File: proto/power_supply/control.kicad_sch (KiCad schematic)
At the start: 9 parts, among them J301 Conn_01x04, J302 Conn_01x08, J303 Conn_ARM_JTAG_SWD_20, SW301 SW_Push_Dual, U301 STM32G051C6Tx

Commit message: Finish alim sch, start PCB
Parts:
- SW301: symbol Switch:SW_Push_Dual -> Switch:SW_Push
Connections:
- net GND: no longer SW301.3
- net ~{RST}: no longer SW301.4
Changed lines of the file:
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@@
 (kicad_sch (version 20230221) (generator eeschema)
   (paper "A4")
-  (junction (at 115.57 71.12) (diameter 0) (color 0 0 0 0)
-  )
   (junction (at 166.37 30.48) (diameter 0) (color 0 0 0 0)
   )
@@
   (junction (at 73.025 175.26) (diameter 0) (color 0 0 0 0)
   )
-  (junction (at 115.57 57.15) (diameter 0) (color 0 0 0 0)
-  )
   (junction (at 113.03 57.15) (diameter 0) (color 0 0 0 0)
   )
@@
     (stroke (width 0) (type default))
   )
-  (wire (pts (xy 115.57 57.15) (xy 113.03 57.15))
-    (stroke (width 0) (type default))
-  )
   (wire (pts (xy 180.34 62.23) (xy 203.2 62.23))
     (stroke (width 0) (type default))
@@
     (stroke (width 0) (type default))
   )
-  (wire (pts (xy 115.57 71.12) (xy 123.19 71.12))
-    (stroke (width 0) (type default))
-  )
-  (wire (pts (xy 115.57 57.15) (xy 123.19 57.15))
+  (wire (pts (xy 113.03 57.15) (xy 123.19 57.15))
     (stroke (width 0) (type default))
   )
@@
     (stroke (width 0) (type default))
   )
-  (wire (pts (xy 115.57 69.85) (xy 115.57 71.12))
-    (stroke (width 0) (type default))
-  )
   (wire (pts (xy 142.24 52.07) (xy 149.86 52.07))
     (stroke (width 0) (type default))
@@
     (stroke (width 0) (type default))
   )
-  (wire (pts (xy 115.57 57.15) (xy 115.57 59.69))
-    (stroke (width 0) (type default))
-  )
-  (wire (pts (xy 113.03 71.12) (xy 115.57 71.12))
+  (wire (pts (xy 113.03 71.12) (xy 123.19 71.12))
     (stroke (width 0) (type default))
   )
@@
   (symbol (lib_id "power:+3.3V") (at 173.99 25.4 0) (unit 1)
     (in_bom yes) (on_board yes) (dnp no) (fields_autoplaced)
-    (property "Reference" "#PWR0113" (at 173.99 29.21 0)
+    (property "Reference" "#PWR0301" (at 173.99 29.21 0)
       (effects (font (size 1.27 1.27)) hide)
     )
@@
       (project "power_supply"
         (path "/e87df9ac-84db-475c-955a-f1fa477bbb69/0fb30068-80ae-483e-9171-72d32f48949d"
-          (reference "#PWR0113") (unit 1)
+          (reference "#PWR0301") (unit 1)
         )
       )
@@
   (symbol (lib_id "power:+3.3V") (at 113.03 44.45 0) (unit 1)
     (in_bom yes) (on_board yes) (dnp no) (fields_autoplaced)
-    (property "Reference" "#PWR0116" (at 113.03 48.26 0)
+    (property "Reference" "#PWR0306" (at 113.03 48.26 0)
       (effects (font (size 1.27 1.27)) hide)
     )
@@
       (project "power_supply"
         (path "/e87df9ac-84db-475c-955a-f1fa477bbb69/0fb30068-80ae-483e-9171-72d32f48949d"
-          (reference "#PWR0116") (unit 1)
+          (reference "#PWR0306") (unit 1)
         )
       )
@@
   (symbol (lib_id "power:+3.3V") (at 186.69 25.4 0) (unit 1)
     (in_bom yes) (on_board yes) (dnp no) (fields_autoplaced)
-    (property "Reference" "#PWR0114" (at 186.69 29.21 0)
+    (property "Reference" "#PWR0302" (at 186.69 29.21 0)
       (effects (font (size 1.27 1.27)) hide)
     )
@@
       (project "power_supply"
         (path "/e87df9ac-84db-475c-955a-f1fa477bbb69/0fb30068-80ae-483e-9171-72d32f48949d"
-          (reference "#PWR0114") (unit 1)
+          (reference "#PWR0302") (unit 1)
         )
       )
@@
   (symbol (lib_id "power:+3.3V") (at 50.8 138.43 0) (unit 1)
     (in_bom yes) (on_board yes) (dnp no) (fields_autoplaced)
-    (property "Reference" "#PWR0117" (at 50.8 142.24 0)
+    (property "Reference" "#PWR0310" (at 50.8 142.24 0)
       (effects (font (size 1.27 1.27)) hide)
     )
@@
       (project "power_supply"
         (path "/e87df9ac-84db-475c-955a-f1fa477bbb69/0fb30068-80ae-483e-9171-72d32f48949d"
-          (reference "#PWR0117") (unit 1)
+          (reference "#PWR0310") (unit 1)
         )
       )
@@
   (symbol (lib_id "power:+3.3V") (at 166.37 26.67 0) (unit 1)
     (in_bom yes) (on_board yes) (dnp no) (fields_autoplaced)
-    (property "Reference" "#PWR0115" (at 166.37 30.48 0)
+    (property "Reference" "#PWR0303" (at 166.37 30.48 0)
       (effects (font (size 1.27 1.27)) hide)
     )
@@
       (project "power_supply"
         (path "/e87df9ac-84db-475c-955a-f1fa477bbb69/0fb30068-80ae-483e-9171-72d32f48949d"
-          (reference "#PWR0115") (unit 1)
+          (reference "#PWR0303") (unit 1)
         )
       )
@@
     )
   )
-  (symbol (lib_id "Switch:SW_Push_Dual") (at 110.49 64.77 90) (unit 1)
+  (symbol (lib_id "Switch:SW_Push") (at 110.49 64.77 90) (unit 1)
     (in_bom yes) (on_board yes) (dnp no) (fields_autoplaced)
     (property "Reference" "SW301" (at 106.68 64.135 90)
@@
     (pin "1")
     (pin "2")
-    (pin "3")
-    (pin "4")
-    (instances
-      (project "power_supply"
+    (instances
+      (project "power_supply"

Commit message: Improve overall
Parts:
- added C304, C305: C, Capacitor_SMD:C_0805_2012Metric, symbol Device:C
- added J304: Conn_01x03, Connector_PinHeader_2.54mm:PinHeader_1x03_P2.54mm_Horizontal, symbol Connector_Generic:Conn_01x03
- added R302: 0, Resistor_SMD:R_0805_2012Metric, symbol Device:R
- added Y301: 8MHz, Crystal:Crystal_SMD_5032-2Pin_5.0x3.2mm, symbol Device:Crystal
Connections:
- net GND: now also C304.2, C305.2, J304.1 (Pin_1)
- net at U301.29 (PA9/NC): now also J304.3 (Pin_3)
- net at U301.32 (PA10/NC): now also J304.2 (Pin_2)
- net at U301.8 (PF0): now also C305.1, Y301.2
- net at U301.9 (PF1): now also R302.2
- new net: C304.1, R302.1, Y301.1

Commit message: Final edit before v1 release
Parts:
- added D301, D302, D303, D304: LED, LED_SMD:LED_0805_2012Metric, symbol Device:LED
- added R303, R304, R305, R306: 10k, Resistor_SMD:R_0805_2012Metric, symbol Device:R
- J302: value Conn_01x08 -> Conn_01x09; footprint Connector_PinHeader_2.54mm:PinHeader_1x08_P2.54mm_Horizontal -> Connector_PinHeader_2.54mm:PinHeader_1x09_P2.54mm_Horizontal; symbol Connector_Generic:Conn_01x08 -> Connector_Generic:Conn_01x09
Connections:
- net GND: now also J302.9 (Pin_9), D301.1 (K), D302.1 (K), D303.1 (K), D304.1 (K)
- net at U301.38 (PD0): now also R306.1
- net at U301.39 (PD1): now also R305.1
- net at U301.40 (PD2): now also R304.1
- net at U301.41 (PD3): now also R303.1
- new net: D303.2 (A), R305.2
- new net: D304.2 (A), R306.2
- new net: D301.2 (A), R303.2
- new net: D302.2 (A), R304.2
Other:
- moved on the sheet: C303, R301, SW301

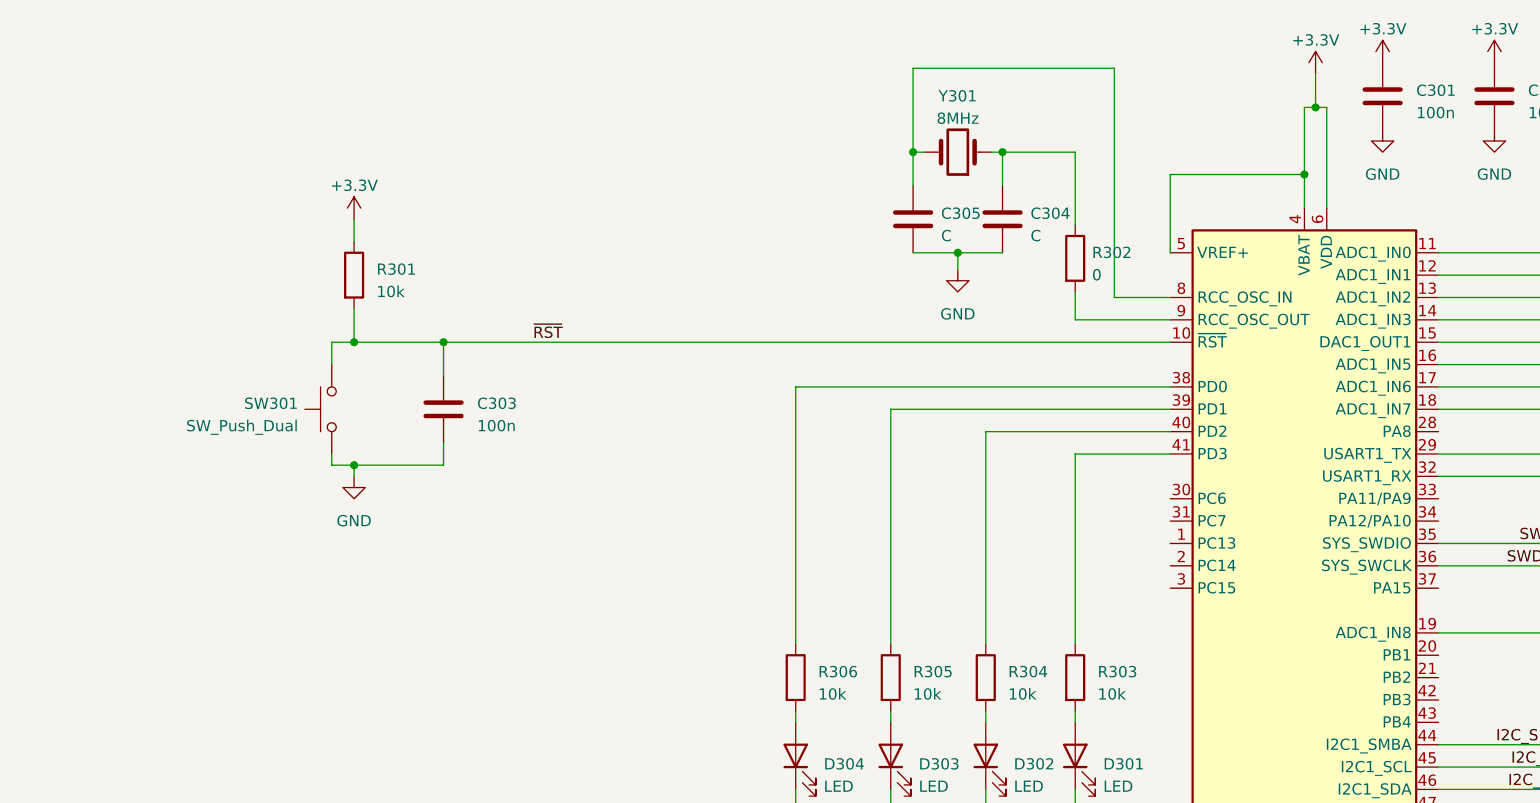
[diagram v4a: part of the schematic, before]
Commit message: Update for BOM
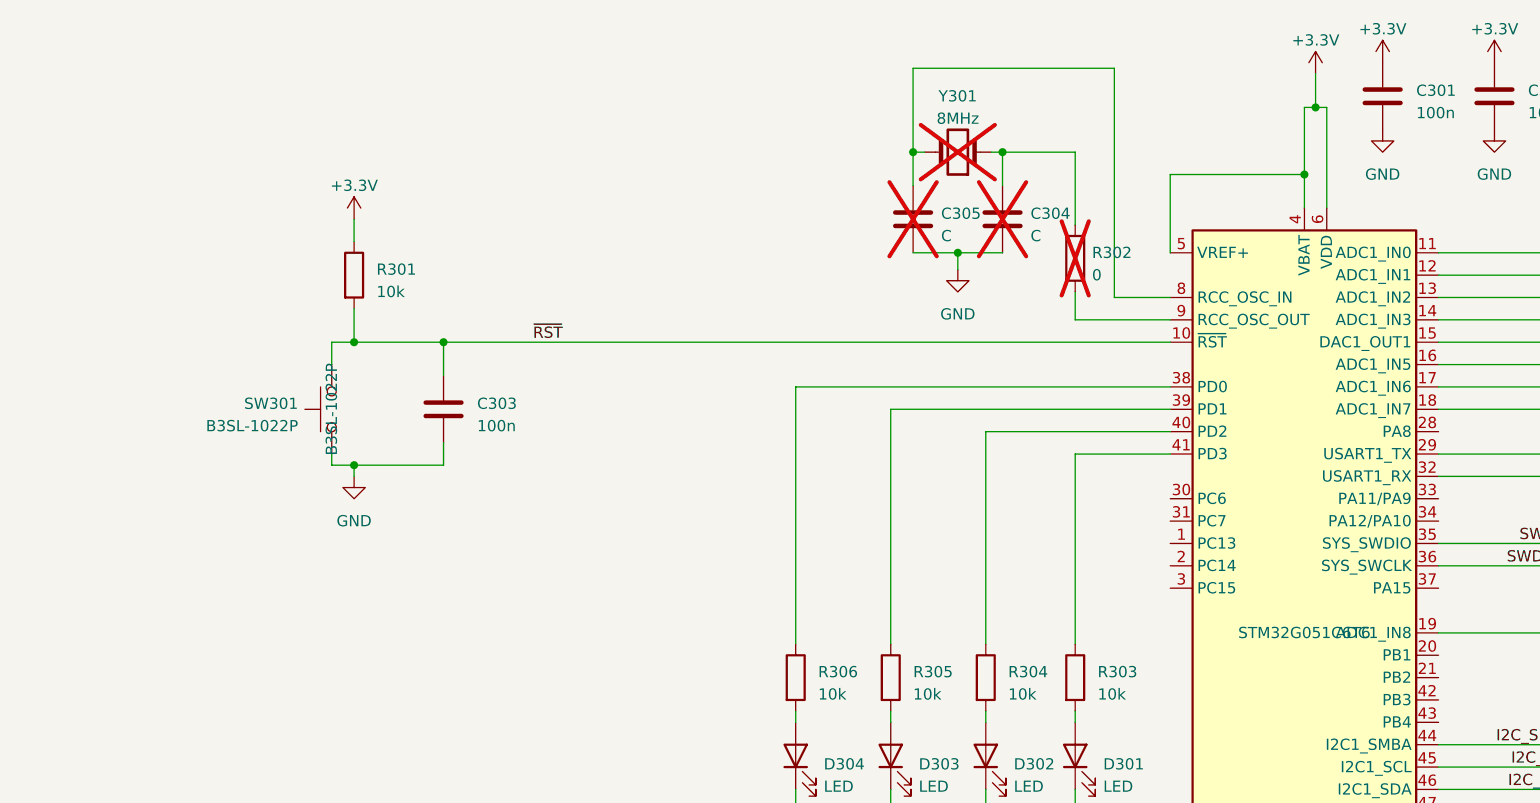
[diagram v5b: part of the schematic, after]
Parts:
- C304, C305, R302, Y301: now not fitted; now left out of the parts list
- D301, D302, D303, D304: now left out of the parts list
- SW301: value SW_Push_Dual -> B3SL-1022P; MPN (none) -> B3SL-1022P
- U301: MPN (none) -> STM32G051C6T6
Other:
- company: (none) -> Julien FAUCHER
- title: (none) -> MPPT - PSU : MCU
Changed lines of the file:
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@@
 (kicad_sch (version 20230221) (generator eeschema)
   (paper "A4")
+  (title_block
+    (title "MPPT - PSU : MCU")
+    (date "2023-04-05")
+    (rev "Rev. 1.0")
+    (company "Julien FAUCHER")
+    (comment 1 "Defis solaires 2023")
+  )
   (junction (at 128.905 113.03) (diameter 0) (color 0 0 0 0)
   )
@@
   )
   (symbol (lib_id "Device:LED") (at 118.11 104.14 90) (unit 1)
-    (in_bom yes) (on_board yes) (dnp no) (fields_autoplaced)
+    (in_bom no) (on_board yes) (dnp no) (fields_autoplaced)
     (property "Reference" "D303" (at 121.285 105.0925 90)
       (effects (font (size 1.27 1.27)) (justify right))
@@
       (effects (font (size 1.27 1.27)) hide)
     )
+    (property "MPN" "" (at 118.11 104.14 0)
+      (effects (font (size 1.27 1.27)))
+    )
     (pin "1")
     (pin "2")
@@
   )
   (symbol (lib_id "Device:LED") (at 107.315 104.14 90) (unit 1)
-    (in_bom yes) (on_board yes) (dnp no) (fields_autoplaced)
+    (in_bom no) (on_board yes) (dnp no) (fields_autoplaced)
     (property "Reference" "D304" (at 110.49 105.0925 90)
       (effects (font (size 1.27 1.27)) (justify right))
@@
       (effects (font (size 1.27 1.27)) hide)
     )
+    (property "MPN" "" (at 107.315 104.14 0)
+      (effects (font (size 1.27 1.27)))
+    )
     (pin "1")
     (pin "2")
@@
   )
   (symbol (lib_id "Device:C") (at 130.81 43.18 0) (unit 1)
-    (in_bom yes) (on_board yes) (dnp no) (fields_autoplaced)
+    (in_bom no) (on_board yes) (dnp yes) (fields_autoplaced)
     (property "Reference" "C304" (at 133.985 42.545 0)
       (effects (font (size 1.27 1.27)) (justify left))
@@
     (property "Datasheet" "~" (at 130.81 43.18 0)
       (effects (font (size 1.27 1.27)) hide)
+    )
+    (property "MPN" "" (at 130.81 43.18 0)
+      (effects (font (size 1.27 1.27)))
     )
     (pin "1")
@@
   )
   (symbol (lib_id "Device:R") (at 139.065 47.625 0) (unit 1)
-    (in_bom yes) (on_board yes) (dnp no) (fields_autoplaced)
+    (in_bom no) (on_board yes) (dnp yes) (fields_autoplaced)
     (property "Reference" "R302" (at 140.97 46.99 0)
       (effects (font (size 1.27 1.27)) (justify left))
@@
       (effects (font (size 1.27 1.27)) hide)
     )
+    (property "MPN" "" (at 139.065 47.625 0)
+      (effects (font (size 1.27 1.27)))
+    )
     (pin "1")
     (pin "2")
@@
   )
   (symbol (lib_id "Device:C") (at 120.65 43.18 0) (unit 1)
-    (in_bom yes) (on_board yes) (dnp no) (fields_autoplaced)
+    (in_bom no) (on_board yes) (dnp yes) (fields_autoplaced)
     (property "Reference" "C305" (at 123.825 42.545 0)
       (effects (font (size 1.27 1.27)) (justify left))
@@
       (effects (font (size 1.27 1.27)) hide)
     )
+    (property "MPN" "" (at 120.65 43.18 0)
+      (effects (font (size 1.27 1.27)))
+    )
     (pin "1")
     (pin "2")
@@
   )
   (symbol (lib_id "Device:LED") (at 128.905 104.14 90) (unit 1)
-    (in_bom yes) (on_board yes) (dnp no) (fields_autoplaced)
+    (in_bom no) (on_board yes) (dnp no) (fields_autoplaced)
     (property "Reference" "D302" (at 132.08 105.0925 90)
       (effects (font (size 1.27 1.27)) (justify right))
@@
       (effects (font (size 1.27 1.27)) hide)
     )
+    (property "MPN" "" (at 128.905 104.14 0)
+      (effects (font (size 1.27 1.27)))
+    )
     (pin "1")
     (pin "2")
@@
   )
   (symbol (lib_id "Device:LED") (at 139.065 104.14 90) (unit 1)
-    (in_bom yes) (on_board yes) (dnp no) (fields_autoplaced)
+    (in_bom no) (on_board yes) (dnp no) (fields_autoplaced)
     (property "Reference" "D301" (at 142.24 105.0925 90)
       (effects (font (size 1.27 1.27)) (justify right))
@@
     (property "Datasheet" "~" (at 139.065 104.14 0)
       (effects (font (size 1.27 1.27)) hide)
+    )
+    (property "MPN" "" (at 139.065 104.14 0)
+      (effects (font (size 1.27 1.27)))
     )
     (pin "1")
@@
   )
   (symbol (lib_id "Device:Crystal") (at 125.73 35.56 180) (unit 1)
-    (in_bom yes) (on_board yes) (dnp no) (fields_autoplaced)
+    (in_bom no) (on_board yes) (dnp yes) (fields_autoplaced)
     (property "Reference" "Y301" (at 125.73 29.21 0)
       (effects (font (size 1.27 1.27)))
@@
     (property "Datasheet" "~" (at 125.73 35.56 0)
       (effects (font (size 1.27 1.27)) hide)
+    )
+    (property "MPN" "" (at 125.73 35.56 0)
+      (effects (font (size 1.27 1.27)))
     )
     (pin "1")
@@
       (effects (font (size 1.27 1.27)) hide)
     )
-    (property "MPN" "" (at 165.1 90.17 0)
+    (property "MPN" "STM32G051C6T6" (at 165.1 90.17 0)
       (effects (font (size 1.27 1.27)))
     )
@@
       (effects (font (size 1.27 1.27)) (justify left))
     )
-    (property "Value" "SW_Push_Dual" (at 50.8 66.675 90)
+    (property "Value" "B3SL-1022P" (at 50.8 66.675 90)
       (effects (font (size 1.27 1.27)) (justify left))
     )
@@
       (effects (font (size 1.27 1.27)) hide)
     )
-    (property "MPN" "" (at 54.61 64.77 0)
-      (effects (font (size 1.27 1.27)))
-    )
+    (property "MPN" "B3SL-1022P" (at 54.61 64.77 0)
+      (effects (font (size 1.27 1.27)))
+    )
